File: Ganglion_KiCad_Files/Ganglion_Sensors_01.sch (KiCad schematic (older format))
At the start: 25 parts, among them U12 AD5621, U13 SEEED_microSD, U14 MCP6V13T, U15 MCP6001, U16 SN74LVC1G32, U17 LIS2DE12, U18 74LVC1G66, U19 74LVC1G66, U20 74LVC1G66, U21 74LVC1G66, U22 74LVC1G66, U23 74LVC2G00

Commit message: Annotate components with manufacturer part numbers
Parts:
- C35: ManufacturerPartNumber (none) -> GRM21BR60J476ME15L
- C36: ManufacturerPartNumber (none) -> GCM188R71H103KA37D
- C40, C42: ManufacturerPartNumber (none) -> GRM188R61E105KA12D
- C41: ManufacturerPartNumber (none) -> GRM188C80G106ME47D
- R39: ManufacturerPartNumber (none) -> ERJ-3EKF1000V
- R40, R41: ManufacturerPartNumber (none) -> ERJ-3EKF1001V
- R42, R43: ManufacturerPartNumber (none) -> ERJ-3EKF1004V
- R44, R45, R46: ManufacturerPartNumber (none) -> ERJ-3EKF1003V
- U12: ManufacturerPartNumber (none) -> AD5621AKSZ-REEL7
- U13: ManufacturerPartNumber (none) -> ST-TF-003A
- U14: ManufacturerPartNumber (none) -> MCP6V31T-E/OT
- U15: ManufacturerPartNumber (none) -> MCP6001T-I/LT
- U16: ManufacturerPartNumber (none) -> SN74LVC1G32DCKR
- U17: ManufacturerPartNumber (none) -> LIS2DE12TR
- U18, U19, U20, U21, U22: ManufacturerPartNumber (none) -> 74LVC1G66GW,125
- U23: ManufacturerPartNumber (none) -> SN74LVC2G00DCUR
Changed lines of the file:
@@
 F 2 "OpenBCI:LIS2DH12" H 3950 5700 60  0001 C CNN
 F 3 "" H 3950 5700 60  0000 C CNN
+F 4 "LIS2DE12TR" H 3750 6050 60  0001 C CNN "ManufacturerPartNumber"
 	1    3750 6050
 	1    0    0    -1
@@
 F 2 "TO_SOT_Packages_SMD:SC-70-5" H 2350 6150 50  0001 C CNN
 F 3 "" H 2350 6150 50  0000 C CNN
+F 4 "SN74LVC1G32DCKR" H 2350 6150 60  0001 C CNN "ManufacturerPartNumber"
 	1    2350 6150
 	1    0    0    -1
@@
 F 2 "Capacitors_SMD:C_0603" H 3538 6800 50  0001 C CNN
 F 3 "" H 3500 6950 50  0000 C CNN
+F 4 "GRM188C80G106ME47D" H 3500 6950 60  0001 C CNN "ManufacturerPartNumber"
 	1    3500 6950
 	1    0    0    -1
@@
 F 2 "Capacitors_SMD:C_0603" H 3988 6800 50  0001 C CNN
 F 3 "" H 3950 6950 50  0000 C CNN
+F 4 "GRM188R61E105KA12D" H 3950 6950 60  0001 C CNN "ManufacturerPartNumber"
 	1    3950 6950
 	1    0    0    -1
@@
 F 2 "TO_SOT_Packages_SMD:SC-70-6" H 1800 3550 50  0001 C CIN
 F 3 "" H 1800 3550 50  0000 C CNN
+F 4 "AD5621AKSZ-REEL7" H 1800 3550 60  0001 C CNN "ManufacturerPartNumber"
 	1    1800 3550
 	-1   0    0    -1
@@
 F 2 "TO_SOT_Packages_SMD:SC-70-5" H 4900 3650 50  0001 C CNN
 F 3 "" H 5000 3750 50  0000 C CNN
+F 4 "MCP6001T-I/LT" H 4950 3550 60  0001 C CNN "ManufacturerPartNumber"
 	1    4950 3550
 	-1   0    0    -1
@@
 F 2 "TO_SOT_Packages_SMD:SOT-23-5" H 3550 4000 50  0001 C CNN
 F 3 "" H 3650 4100 50  0000 C CNN
+F 4 "MCP6V31T-E/OT" H 3600 3900 60  0001 C CNN "ManufacturerPartNumber"
 	1    3600 3900
 	1    0    0    -1
@@
 F 2 "Resistors_SMD:R_0603" V 2630 3900 50  0001 C CNN
 F 3 "" H 2700 3900 50  0000 C CNN
+F 4 "ERJ-3EKF1000V" H 2700 3900 60  0001 C CNN "ManufacturerPartNumber"
 	1    2700 3900
 	1    0    0    -1
@@
 F 2 "Resistors_SMD:R_0603" V 2880 3550 50  0001 C CNN
 F 3 "" H 2950 3550 50  0000 C CNN
+F 4 "ERJ-3EKF1001V" V 2950 3550 60  0001 C CNN "ManufacturerPartNumber"
 	1    2950 3550
 	0    1    1    0
@@
 F 2 "Resistors_SMD:R_0603" V 2880 4300 50  0001 C CNN
 F 3 "" H 2950 4300 50  0000 C CNN
+F 4 "ERJ-3EKF1001V" V 2950 4300 60  0001 C CNN "ManufacturerPartNumber"
 	1    2950 4300
 	0    1    1    0
@@
 F 2 "Resistors_SMD:R_0603" V 3730 3550 50  0001 C CNN
 F 3 "" H 3800 3550 50  0000 C CNN
+F 4 "ERJ-3EKF1004V" H 3800 3550 60  0001 C CNN "ManufacturerPartNumber"
 	1    3800 3550
 	0    1    1    0
@@
 F 2 "Resistors_SMD:R_0603" V 3730 4300 50  0001 C CNN
 F 3 "" H 3800 4300 50  0000 C CNN
+F 4 "ERJ-3EKF1004V" H 3800 4300 60  0001 C CNN "ManufacturerPartNumber"
 	1    3800 4300
 	0    1    1    0
@@
 F 2 "Resistors_SMD:R_0603" V 5330 3200 50  0001 C CNN
 F 3 "" H 5400 3200 50  0000 C CNN
+F 4 "ERJ-3EKF1003V" V 5400 3200 60  0001 C CNN "ManufacturerPartNumber"
 	1    5400 3200
 	0    -1   -1   0
@@
 F 2 "Resistors_SMD:R_0603" V 5580 3750 50  0001 C CNN
 F 3 "" H 5650 3750 50  0000 C CNN
+F 4 "ERJ-3EKF1003V" V 5650 3750 60  0001 C CNN "ManufacturerPartNumber"
 	1    5650 3750
 	1    0    0    -1
@@
 F 2 "Capacitors_SMD:C_0603" H 5938 3600 50  0001 C CNN
 F 3 "" H 5900 3750 50  0000 C CNN
+F 4 "GRM188R61E105KA12D" H 5900 3750 60  0001 C CNN "ManufacturerPartNumber"
 	1    5900 3750
 	1    0    0    -1
@@
 F 2 "OpenBCI:ST-TF-0003A" H 2500 2250 60  0001 C CNN
 F 3 "" H 2500 2250 60  0000 C CNN
+F 4 "ST-TF-003A" H 2250 1650 60  0001 C CNN "ManufacturerPartNumber"
 	1    2250 1650
 	1    0    0    -1
@@
 F 2 "Capacitors_SMD:C_1210" H 1538 1300 50  0001 C CNN
 F 3 "" H 1500 1450 50  0000 C CNN
+F 4 "GRM21BR60J476ME15L" H 1500 1450 60  0001 C CNN "ManufacturerPartNumber"
 	1    1500 1450
 	-1   0    0    1
@@
 F 2 "TO_SOT_Packages_SMD:SC-70-5" H 9750 4600 60  0001 C CNN
 F 3 "" H 9750 4600 60  0000 C CNN
+F 4 "74LVC1G66GW,125" H 9750 4600 60  0001 C CNN "ManufacturerPartNumber"
 	1    9750 4600
 	1    0    0    -1
@@
 F 2 "TO_SOT_Packages_SMD:SC-70-5" H 8700 3500 60  0001 C CNN
 F 3 "" H 8700 3500 60  0000 C CNN
+F 4 "74LVC1G66GW,125" H 8700 3500 60  0001 C CNN "ManufacturerPartNumber"
 	1    8700 3500
 	1    0    0    -1
@@
 F 2 "TO_SOT_Packages_SMD:SC-70-5" H 7700 4600 60  0001 C CNN
 F 3 "" H 7700 4600 60  0000 C CNN
+F 4 "74LVC1G66GW,125" H 7700 4600 60  0001 C CNN "ManufacturerPartNumber"
 	1    7700 4600
 	1    0    0    -1
@@
 F 2 "TO_SOT_Packages_SMD:SC-70-5" H 7700 5800 60  0001 C CNN
 F 3 "" H 7700 5800 60  0000 C CNN
+F 4 "74LVC1G66GW,125" H 7700 5800 60  0001 C CNN "ManufacturerPartNumber"
 	1    7700 5800
 	1    0    0    -1
@@
 F 2 "TO_SOT_Packages_SMD:SC-70-5" H 9750 5800 60  0001 C CNN
 F 3 "" H 9750 5800 60  0000 C CNN
+F 4 "74LVC1G66GW,125" H 9750 5800 60  0001 C CNN "ManufacturerPartNumber"
 	1    9750 5800
 	1    0    0    -1
@@
 F 2 "OpenBCI:VSSOP-8" H 5750 1600 50  0001 C CNN
 F 3 "" H 5750 1600 50  0000 C CNN
+F 4 "SN74LVC2G00DCUR" H 5750 1600 60  0001 C CNN "ManufacturerPartNumber"
 	1    5750 1600
 	1    0    0    -1
@@
 F 2 "OpenBCI:VSSOP-8" H 8100 1600 50  0001 C CNN
 F 3 "" H 8100 1600 50  0000 C CNN
+F 4 "SN74LVC2G00DCUR" H 8100 1600 60  0001 C CNN "ManufacturerPartNumber"
 	2    8100 1600
 	1    0    0    -1
@@
 F 2 "Capacitors_SMD:C_0603" H 6688 1450 50  0001 C CNN
 F 3 "" H 6650 1600 50  0000 C CNN
+F 4 "GCM188R71H103KA37D" H 6650 1600 60  0001 C CNN "ManufacturerPartNumber"
 	1    6650 1600
 	0    -1   -1   0
@@
 F 2 "Resistors_SMD:R_0603" V 6930 1850 50  0001 C CNN
 F 3 "" H 7000 1850 50  0000 C CNN
+F 4 "ERJ-3EKF1003V" V 7000 1850 60  0001 C CNN "ManufacturerPartNumber"
 	1    7000 1850
 	1    0    0    -1

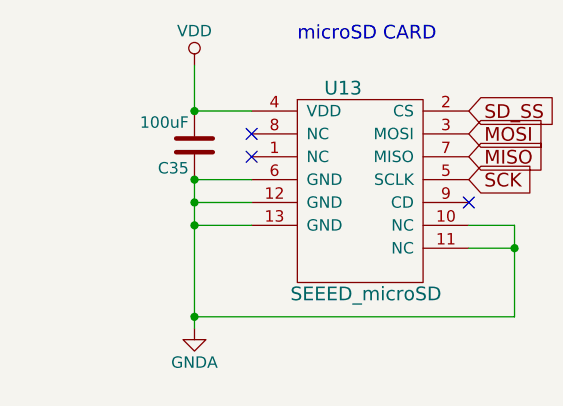
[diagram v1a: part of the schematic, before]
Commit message: Fix discrepancies between schematic/board values and the BOM
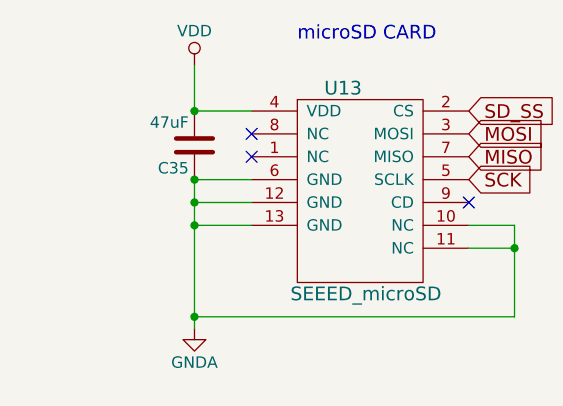
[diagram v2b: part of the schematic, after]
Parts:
- C35: value 100uF -> 47uF
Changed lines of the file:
@@
 P 1500 1450
 F 0 "C35" H 1525 1550 50  0000 L CNN
-F 1 "100uF" H 1525 1350 50  0000 L CNN
+F 1 "47uF" H 1525 1350 50  0000 L CNN
 F 2 "Capacitors_SMD:C_1210" H 1538 1300 50  0001 C CNN
 F 3 "" H 1500 1450 50  0000 C CNN
